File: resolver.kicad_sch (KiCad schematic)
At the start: 40 parts, among them Q1 BD135, Q2 BD136, Q3 BD135, Q4 BD136, U1 AD2S1205, U2 LM358, Y1 Crystal

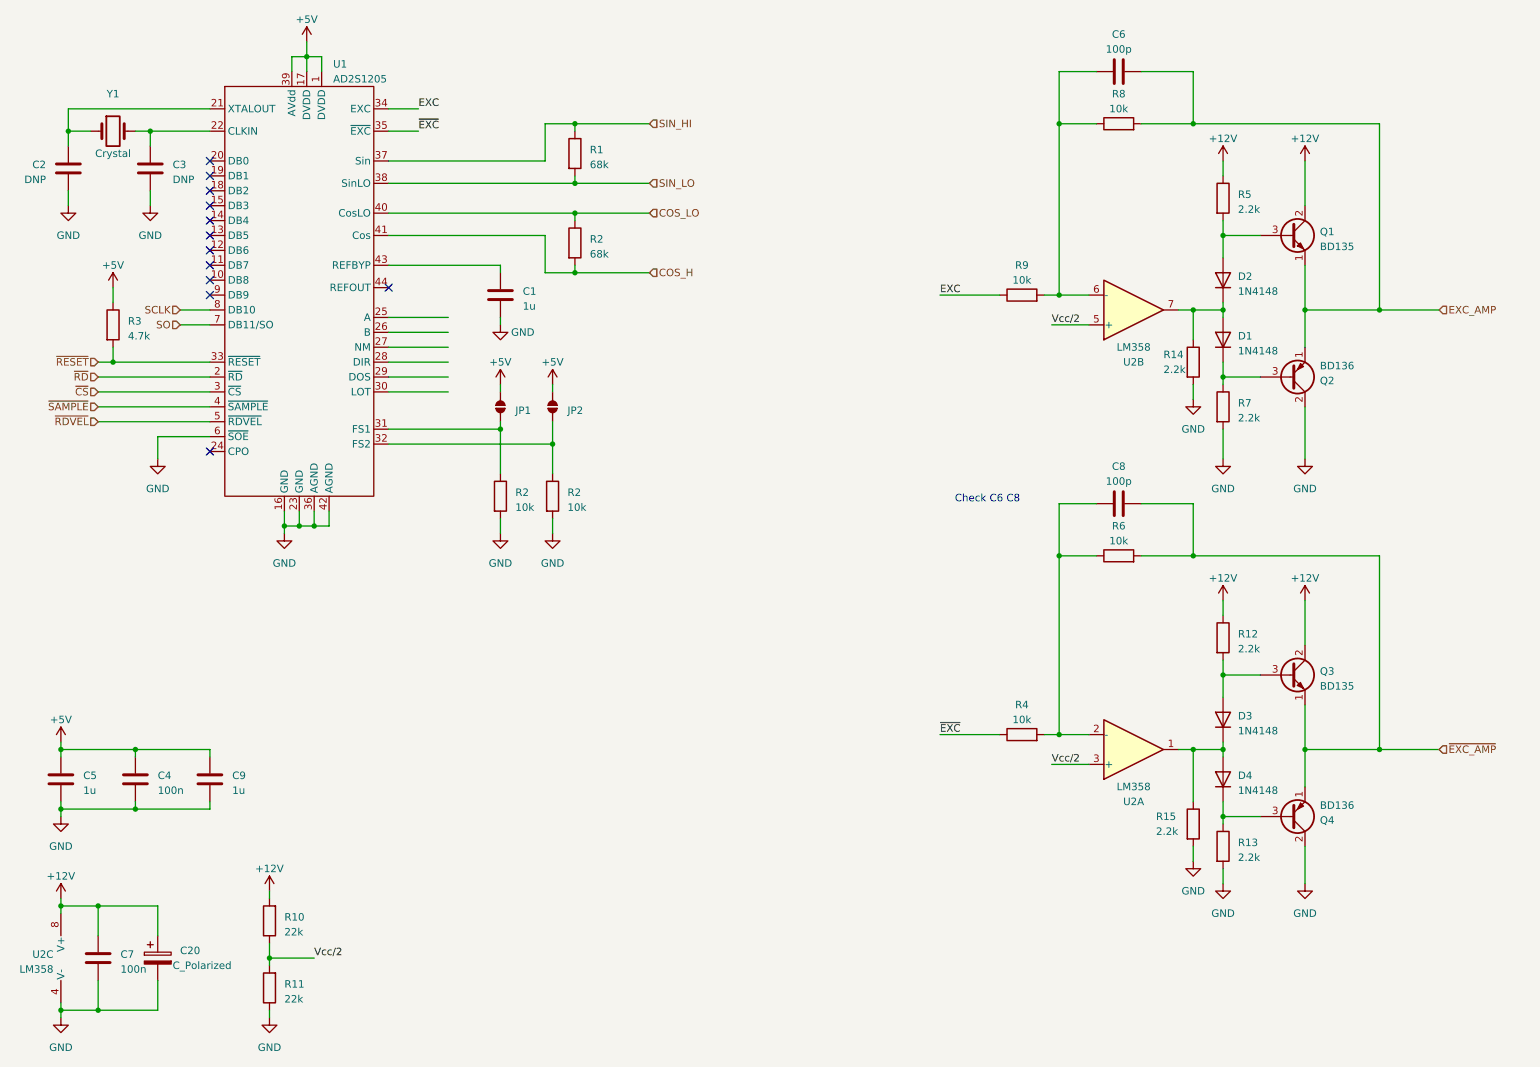
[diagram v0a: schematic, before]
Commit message: Added current sensing
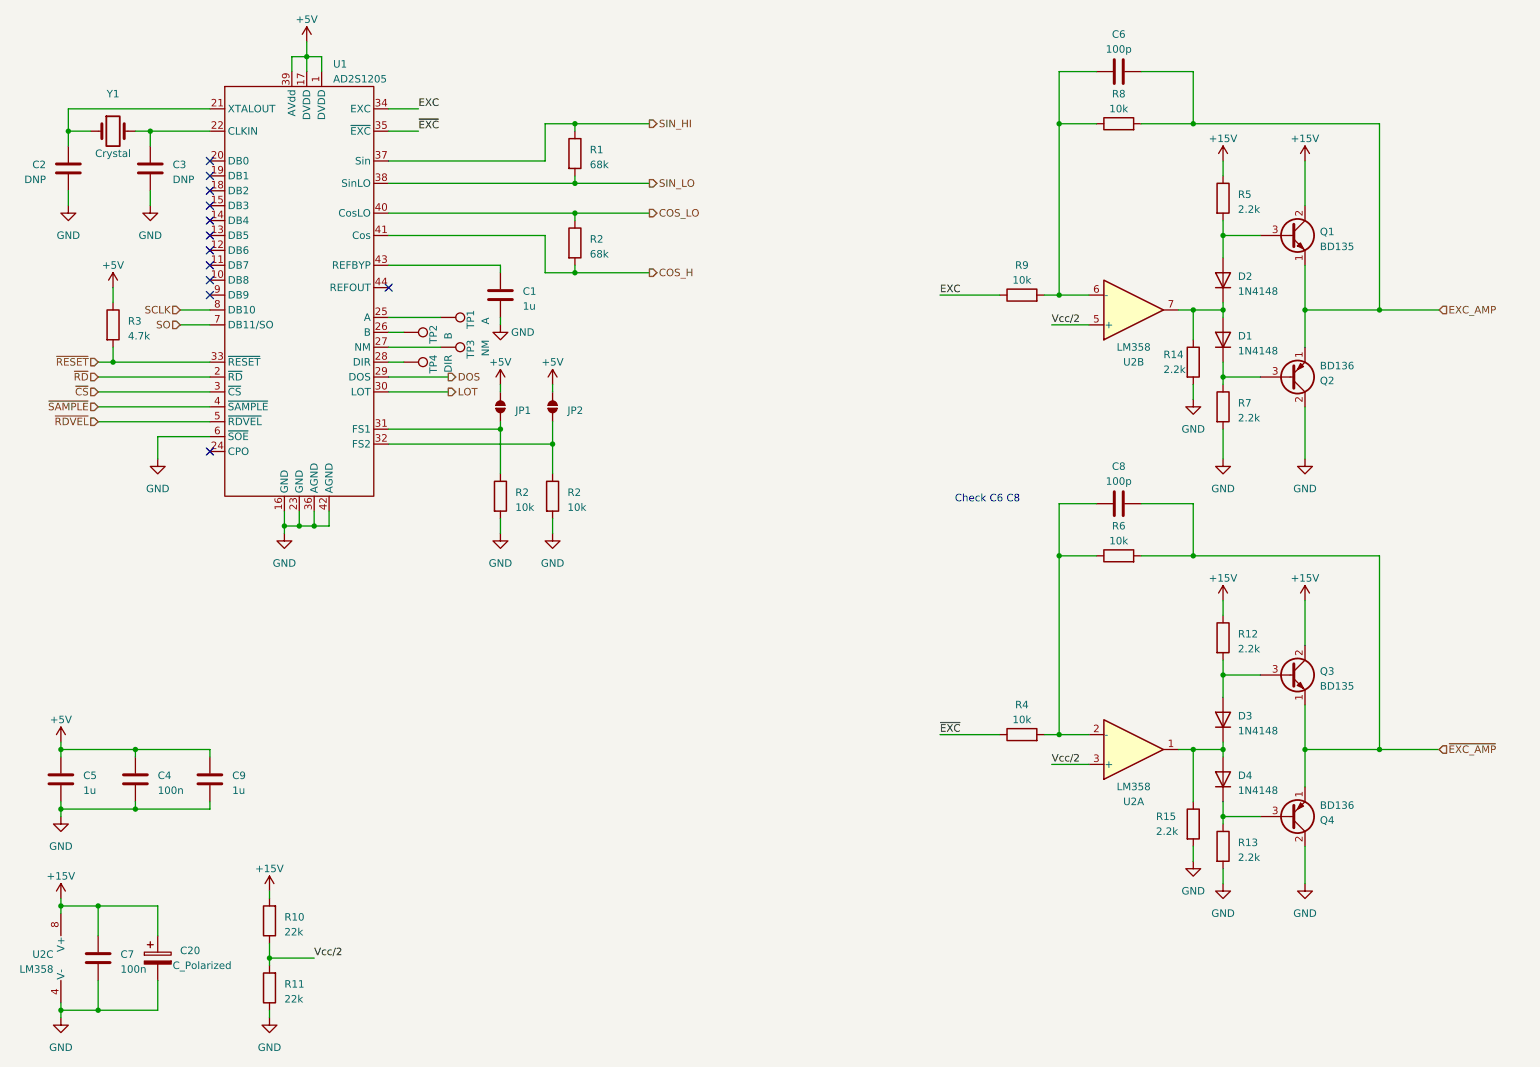
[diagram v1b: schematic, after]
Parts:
- added TP1: A, symbol Connector:TestPoint
- added TP2: B, symbol Connector:TestPoint
- added TP3: NM, symbol Connector:TestPoint
- added TP4: DIR, symbol Connector:TestPoint
- D3: footprint Diode_SMD:D_SMA_Handsoldering -> (none)
- Q1, Q2, Q3, Q4: footprint Package_TO_SOT_THT:TO-126-3_Vertical -> (none)
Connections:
- net at U1.25 (A): now also TP1.1
- net at U1.26 (B): now also TP2.1
- net at U1.27 (NM): now also TP3.1
- net at U1.28 (DIR): now also TP4.1
- net DOS: now reaches U1.29 (DOS)
- net LOT: now reaches U1.30 (LOT)
- net +12V renamed +15V

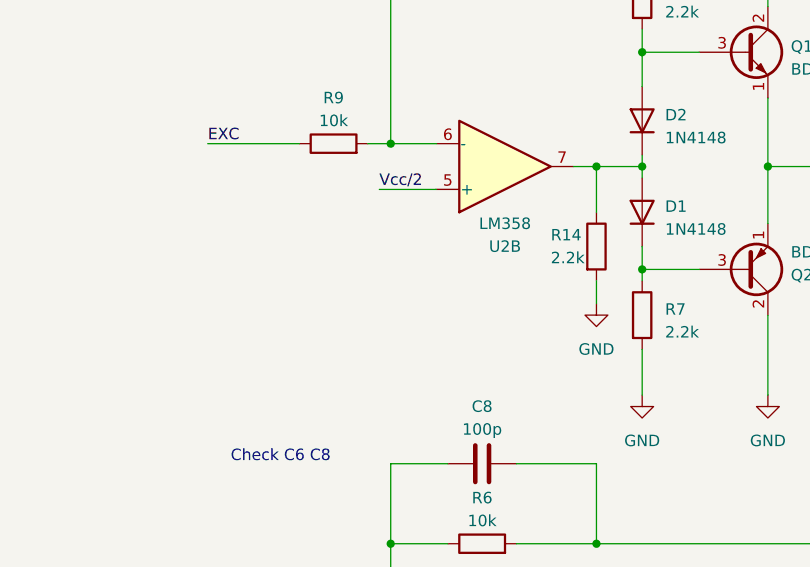
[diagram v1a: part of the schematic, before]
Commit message: Connectors added
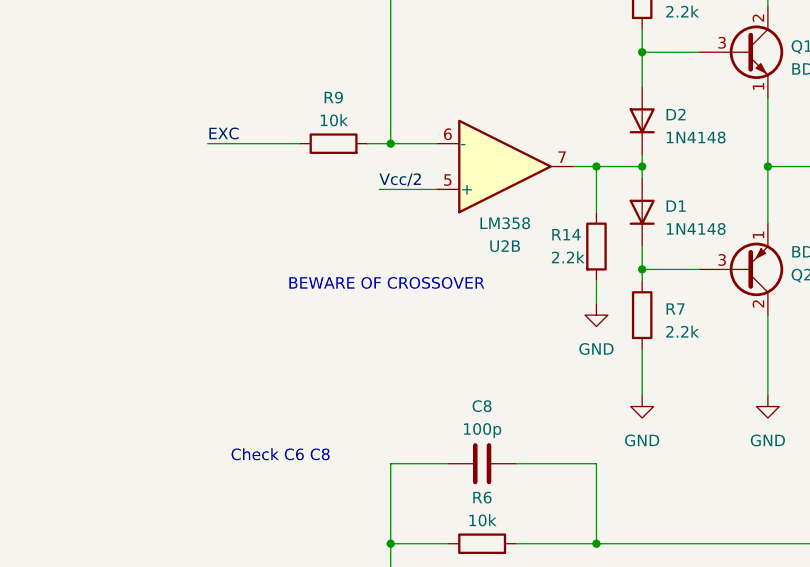
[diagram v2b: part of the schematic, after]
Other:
- note added: "BEWARE OF CROSSOVER"
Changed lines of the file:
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@@
+    (effects (font (size 1.27 1.27)) (justify left bottom))
+  )
+  (text "BEWARE OF CROSSOVER " (at 186.69 78.74 0)
     (effects (font (size 1.27 1.27)) (justify left bottom))
   )

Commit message: Footprints
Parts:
- removed D1, D2, D4: 1N4148, Diode_SMD:D_SMA_Handsoldering, symbol Diode:1N4148
- removed D3: 1N4148, symbol Diode:1N4148
- removed Q1, Q3: BD135, symbol Transistor_BJT:BD135
- removed Q2, Q4: BD136, symbol Transistor_BJT:BD136
- added D1, D2, D3, D8: 1N4148, Diode_SMD:D_SOD-323F, symbol MEMS_Discrete_Semiconductors:D_1N4148WS-SOD323
- added Q1, Q5: BCX54, Package_TO_SOT_SMD:SOT-89-3, symbol Device:Q_NPN_BCE
- added Q2, Q6: BCX55, Package_TO_SOT_SMD:SOT-89-3, symbol Device:Q_PNP_BCE
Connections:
- net +15V: now also Q1.2 (C), Q5.2 (C)
- net EXC_AMP: now also Q5.3 (E), Q6.2 (C)
- net GND: now also Q2.3 (E), Q6.3 (E)
- net ~{EXC_AMP}: now also Q1.3 (E), Q2.2 (C)
- net at R15.1, U2.1: now also D2.1 (K), D3.2 (A)
- net at R14.1, U2.7: now also D1.2 (A), D8.1 (K)
- net at R13.1: now also D3.1 (K), Q2.1 (B)
- net at R12.2: now also D2.2 (A), Q1.1 (B)
- net at R5.2: now also D8.2 (A), Q5.1 (B)
- net at R7.1: now also D1.1 (K), Q6.1 (B)

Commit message: Preliminary footprints
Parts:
- removed C1, C5, C9: 1u, Capacitor_SMD:C_0805_2012Metric_Pad1.18x1.45mm_HandSolder, symbol Device:C
- removed C4: 100n, Capacitor_SMD:C_0805_2012Metric_Pad1.18x1.45mm_HandSolder, symbol Device:C
- removed Y1: Crystal, Crystal:Crystal_HC49-U_Vertical, symbol Device:Crystal
- added C1 (x3): 1u, Capacitor_SMD:C_0402_1005Metric_Pad0.74x0.62mm_HandSolder, symbol Device:C
- added Y3: CSTNE8M00GH5C000R0, Crystal:Resonator_SMD_Murata_CSTxExxV-3Pin_3.0x1.1mm_HandSoldering, symbol Device:Crystal_GND2
- C2, C3: footprint Capacitor_SMD:C_0805_2012Metric_Pad1.18x1.45mm_HandSolder -> Capacitor_SMD:C_0603_1608Metric_Pad1.08x0.95mm_HandSolder
- C20: value C_Polarized -> 100u; footprint (none) -> Capacitor_SMD:CP_Elec_6.3x7.7
- D1, D2, D3, D8: footprint Diode_SMD:D_SOD-323F -> Diode_SMD:D_SOD-323; LCSC (none) -> C727111
- Q1, Q5: LCSC (none) -> C475647
- Q2, Q6: LCSC (none) -> C475649
- R1, R10, R11, R12, R13, R14, R15, R2, R3, R4, R5, R6, R7, R8, R9: footprint Resistor_SMD:R_0805_2012Metric -> Resistor_SMD:R_0603_1608Metric_Pad0.98x0.95mm_HandSolder
- TP1, TP2, TP3, TP4: footprint (none) -> TestPoint:TestPoint_Pad_D1.0mm
- U2: LCSC (none) -> C9418
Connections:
- net +5V: now also C1.1, C1.1
- net GND: now also C1.2, C1.2, C1.2, Y3.2
- net at U1.43 (REFBYP): now also C1.1
- net at C2.1, U1.21 (XTALOUT): now also Y3.1
- net at C3.1, U1.22 (CLKIN): now also Y3.3

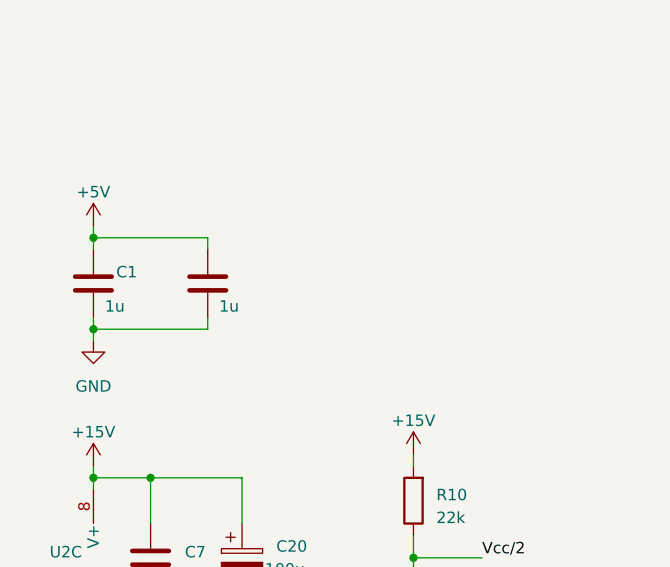
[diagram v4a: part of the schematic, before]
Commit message: Resolver layout
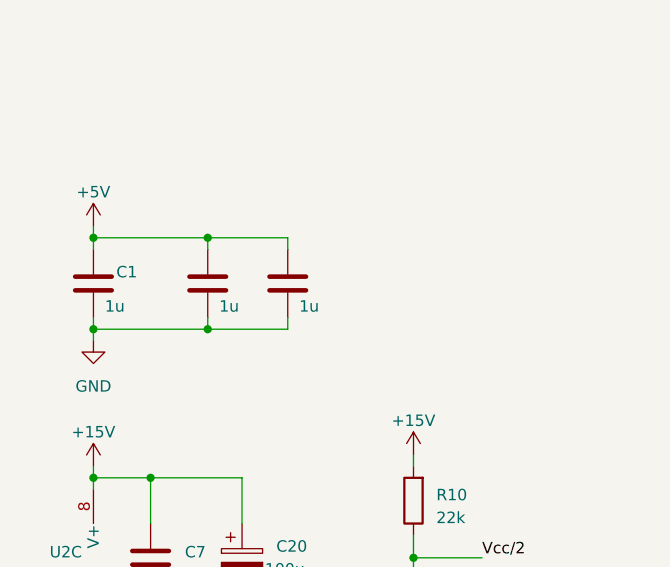
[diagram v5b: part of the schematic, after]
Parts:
- added C1: 1u, Capacitor_SMD:C_0402_1005Metric_Pad0.74x0.62mm_HandSolder, symbol Device:C
- C6, C7, C8: footprint Capacitor_SMD:C_0805_2012Metric_Pad1.18x1.45mm_HandSolder -> Capacitor_SMD:C_0603_1608Metric_Pad1.08x0.95mm_HandSolder
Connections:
- net +5V: now also C1.1
- net GND: now also C1.2
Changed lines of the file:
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@@
   (junction (at 71.12 101.6) (diameter 0) (color 0 0 0 0)
   )
+  (junction (at 40.64 149.86) (diameter 0) (color 0 0 0 0)
+  )
   (junction (at 63.5 175.26) (diameter 0) (color 0 0 0 0)
   )
@@
   )
   (junction (at 69.85 21.59) (diameter 0) (color 0 0 0 0)
+  )
+  (junction (at 40.64 139.7) (diameter 0) (color 0 0 0 0)
   )
   (junction (at 27.94 166.37) (diameter 0) (color 0 0 0 0)
@@
     (stroke (width 0) (type default))
   )
+  (wire (pts (xy 40.64 149.86) (xy 49.53 149.86))
+    (stroke (width 0) (type default))
+  )
   (wire (pts (xy 83.82 85.09) (xy 102.87 85.09))
     (stroke (width 0) (type default))
@@
     (stroke (width 0) (type default))
   )
+  (wire (pts (xy 49.53 148.59) (xy 49.53 149.86))
+    (stroke (width 0) (type default))
+  )
   (wire (pts (xy 110.49 58.42) (xy 115.57 58.42))
     (stroke (width 0) (type default))
@@
     (stroke (width 0) (type default))
   )
+  (wire (pts (xy 49.53 139.7) (xy 49.53 140.97))
+    (stroke (width 0) (type default))
+  )
   (wire (pts (xy 68.58 101.6) (xy 66.04 101.6))
     (stroke (width 0) (type default))
@@
   )
   (wire (pts (xy 66.04 99.06) (xy 66.04 101.6))
+    (stroke (width 0) (type default))
+  )
+  (wire (pts (xy 40.64 139.7) (xy 49.53 139.7))
     (stroke (width 0) (type default))
   )
@@
       (effects (font (size 1.27 1.27)))
     )
-    (property "Footprint" "Capacitor_SMD:C_0805_2012Metric_Pad1.18x1.45mm_HandSolder" (at 212.09 96.8248 0)
+    (property "Footprint" "Capacitor_SMD:C_0603_1608Metric_Pad1.08x0.95mm_HandSolder" (at 212.09 96.8248 0)
       (effects (font (size 1.27 1.27)) hide)
     )
@@
     )
   )
+  (symbol (lib_id "Device:C") (at 49.53 144.78 0) (unit 1)
+    (in_bom yes) (on_board yes) (dnp no)
+    (property "Reference" "C1" (at 52.07 143.51 0)
+      (effects (font (size 1.27 1.27)) (justify left) hide)
+    )
+    (property "Value" "1u" (at 50.8 147.32 0)
+      (effects (font (size 1.27 1.27)) (justify left))
+    )
+    (property "Footprint" "Capacitor_SMD:C_0402_1005Metric_Pad0.74x0.62mm_HandSolder" (at 50.4952 148.59 0)
+      (effects (font (size 1.27 1.27)) hide)
+    )
+    (property "Datasheet" "~" (at 49.53 144.78 0)
+      (effects (font (size 1.27 1.27)) hide)
+    )
+    (property "LCSC" "C126521" (at 49.53 144.78 0)
+      (effects (font (size 1.27 1.27)) hide)
+    )
+    (pin "1")
+    (pin "2")
+    (instances
+      (project "STM32Inverter"
+        (path "/a3442e80-7eef-4b96-92a1-138eb3b79ccb"
+          (reference "C1") (unit 1)
+        )
+        (path "/a3442e80-7eef-4b96-92a1-138eb3b79ccb/8e650c05-dd54-49be-bef9-e4584b0e9ca3"
+          (reference "C31") (unit 1)
+        )
+      )
+    )
+  )
   (symbol (lib_id "Device:R") (at 115.57 38.1 0) (unit 1)
     (in_bom yes) (on_board yes) (dnp no) (fields_autoplaced)
@@
       (effects (font (size 1.27 1.27)) (justify left))
     )
-    (property "Footprint" "Capacitor_SMD:C_0805_2012Metric_Pad1.18x1.45mm_HandSolder" (at 35.2552 179.07 0)
+    (property "Footprint" "Capacitor_SMD:C_0603_1608Metric_Pad1.08x0.95mm_HandSolder" (at 35.2552 179.07 0)
       (effects (font (size 1.27 1.27)) hide)
     )
@@
       (effects (font (size 1.27 1.27)))
     )
-    (property "Footprint" "Capacitor_SMD:C_0805_2012Metric_Pad1.18x1.45mm_HandSolder" (at 212.09 23.1648 0)
-      (effects (font (size 1.27 1.27)) hide)
-    )
+    (property "Footprint" "Capacitor_SMD:C_0603_1608Metric_Pad1.08x0.95mm_HandSolder" (at 212.09 23.1648 0)
+      (effects (font (size 1.27 1.27)) hide)
+    )

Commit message: BOM
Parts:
- C20: LCSC (none) -> C2972718
- C6, C8: Field4 (none) -> mamy; LCSC (none) -> C126576
- C7: LCSC (none) -> C913534
- U1: LCSC (none) -> C55012
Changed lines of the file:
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@@
+      (effects (font (size 1.27 1.27)) hide)
+    )
+    (property "Field4" "mamy" (at 208.28 97.79 0)
+      (effects (font (size 1.27 1.27)) hide)
+    )
+    (property "LCSC" "C126576" (at 208.28 97.79 0)
       (effects (font (size 1.27 1.27)) hide)
     )
@@
       (effects (font (size 1.27 1.27)) hide)
     )
+    (property "LCSC" "C2972718" (at 44.45 175.26 0)
+      (effects (font (size 1.27 1.27)) hide)
+    )
     (pin "1")
     (pin "2")
@@
     )
     (property "Datasheet" "https://www.analog.com/media/en/technical-documentation/data-sheets/AD2S1205.pdf" (at 71.12 25.4 90)
+      (effects (font (size 1.27 1.27)) hide)
+    )
+    (property "LCSC" "C55012" (at 69.85 62.23 0)
       (effects (font (size 1.27 1.27)) hide)
     )
@@
       (effects (font (size 1.27 1.27)) hide)
     )
+    (property "LCSC" "C913534" (at 34.29 175.26 0)
+      (effects (font (size 1.27 1.27)) hide)
+    )
     (pin "1")
     (pin "2")
@@
       (effects (font (size 1.27 1.27)) hide)
     )
+    (property "Field4" "mamy" (at 208.28 24.13 0)
+      (effects (font (size 1.27 1.27)) hide)
+    )
+    (property "LCSC" "C126576" (at 208.28 24.13 0)
+      (effects (font (size 1.27 1.27)) hide)
+    )
